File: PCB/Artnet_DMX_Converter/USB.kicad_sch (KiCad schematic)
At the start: 3 parts, among them J2 USB_C_Receptacle_USB2.0_14P, U3 USBLC6-2SC6

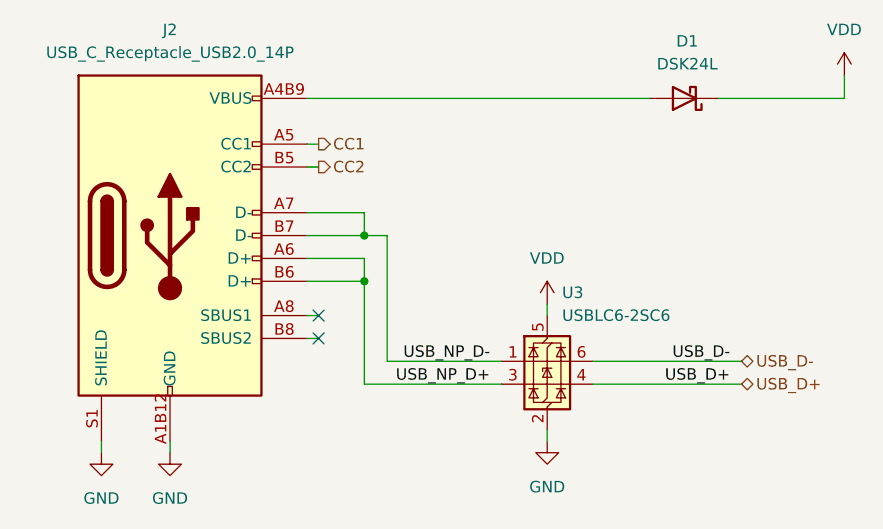
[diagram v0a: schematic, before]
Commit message: Updated the PCB Allot
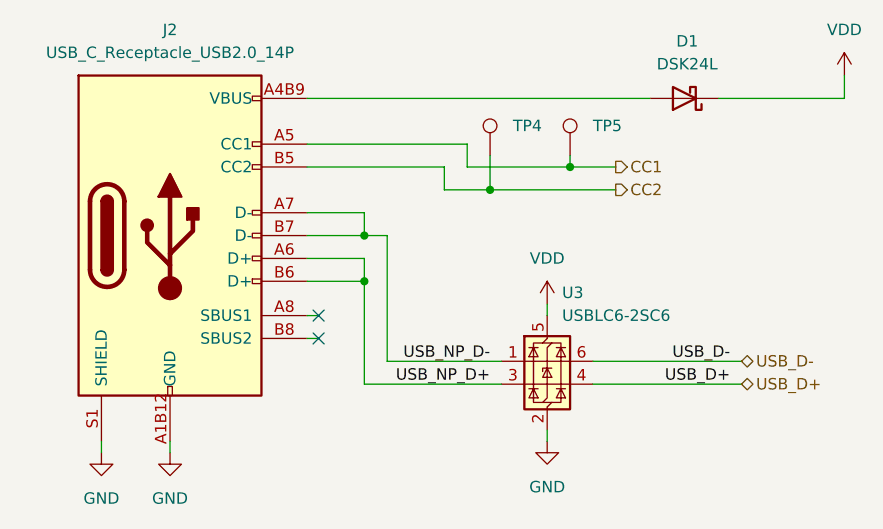
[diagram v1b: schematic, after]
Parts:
- added TP4, TP5: TestPoint, TestPoint:TestPoint_Pad_D1.5mm, symbol Connector:TestPoint
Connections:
- net CC1: now also TP5.1
- net CC2: now also TP4.1
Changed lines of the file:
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@@
+	)
+	(junction
+		(at 125.73 81.28)
+		(diameter 0)
+		(color 0 0 0 0)
 	)
 	(junction
@@
 	)
 	(junction
+		(at 116.84 83.82)
+		(diameter 0)
+		(color 0 0 0 0)
+	)
+	(junction
 		(at 102.87 93.98)
 		(diameter 0)
@@
 	(wire
 		(pts
+			(xy 116.84 83.82) (xy 130.81 83.82)
+		)
+		(stroke
+			(width 0)
+			(type default)
+		)
+	)
+	(wire
+		(pts
 			(xy 102.87 93.98) (xy 102.87 105.41)
 		)
@@
 	(wire
 		(pts
+			(xy 114.3 81.28) (xy 114.3 78.74)
+		)
+		(stroke
+			(width 0)
+			(type default)
+		)
+	)
+	(wire
+		(pts
 			(xy 123.19 111.76) (xy 123.19 110.49)
 		)
@@
 	(wire
 		(pts
-			(xy 96.52 81.28) (xy 97.79 81.28)
+			(xy 111.76 83.82) (xy 116.84 83.82)
 		)
 		(stroke
@@
 	(wire
 		(pts
-			(xy 96.52 78.74) (xy 97.79 78.74)
+			(xy 114.3 81.28) (xy 125.73 81.28)
+		)
+		(stroke
+			(width 0)
+			(type default)
+		)
+	)
+	(wire
+		(pts
+			(xy 96.52 78.74) (xy 114.3 78.74)
 		)
 		(stroke
@@
 	(wire
 		(pts
+			(xy 111.76 83.82) (xy 111.76 81.28)
+		)
+		(stroke
+			(width 0)
+			(type default)
+		)
+	)
+	(wire
+		(pts
 			(xy 96.52 100.33) (xy 97.79 100.33)
 		)
@@
 	(wire
 		(pts
+			(xy 116.84 80.01) (xy 116.84 83.82)
+		)
+		(stroke
+			(width 0)
+			(type default)
+		)
+	)
+	(wire
+		(pts
 			(xy 105.41 88.9) (xy 102.87 88.9)
 		)
@@
 	(wire
 		(pts
+			(xy 125.73 81.28) (xy 130.81 81.28)
+		)
+		(stroke
+			(width 0)
+			(type default)
+		)
+	)
+	(wire
+		(pts
+			(xy 96.52 81.28) (xy 111.76 81.28)
+		)
+		(stroke
+			(width 0)
+			(type default)
+		)
+	)
+	(wire
+		(pts
 			(xy 105.41 102.87) (xy 105.41 88.9)
 		)
@@
 		(pts
 			(xy 96.52 86.36) (xy 102.87 86.36)
+		)
+		(stroke
+			(width 0)
+			(type default)
+		)
+	)
+	(wire
+		(pts
+			(xy 125.73 80.01) (xy 125.73 81.28)
 		)
 		(stroke
@@
 	(hierarchical_label "CC1"
 		(shape output)
-		(at 97.79 78.74 0)
+		(at 130.81 81.28 0)
 		(effects
 			(font
@@
 	(hierarchical_label "CC2"
 		(shape output)
-		(at 97.79 81.28 0)
+		(at 130.81 83.82 0)
 		(effects
 			(font
@@
 		(dnp no)
 		(fields_autoplaced yes)
-		(property "Reference" "#PWR029"
+		(property "Reference" "#PWR027"
 			(at 81.28 119.38 0)
 			(effects
@@
 			(project "Artnet_DMX_Converter"
 				(path "/7d5b1976-98b3-4e47-ae52-3fe360235ea3/29cdc2ff-67bb-4206-b190-ec0480ab55fd"
-					(reference "#PWR029")
+					(reference "#PWR027")
 					(unit 1)
 				)
@@
 	)
 	(symbol
+		(lib_id "Connector:TestPoint")
+		(at 125.73 80.01 0)
+		(unit 1)
+		(exclude_from_sim no)
+		(in_bom yes)
+		(on_board yes)
+		(dnp no)
+		(property "Reference" "TP5"
+			(at 128.27 76.7079 0)
+			(effects
+				(font
+					(size 1.27 1.27)
+				)
+				(justify left)
+			)
+		)
+		(property "Value" "TestPoint"
+			(at 128.27 77.9779 0)
+			(effects
+				(font
+					(size 1.27 1.27)
+				)
+				(justify left)
+				(hide yes)
+			)
+		)
+		(property "Footprint" "TestPoint:TestPoint_Pad_D1.5mm"
+			(at 130.81 80.01 0)
+			(effects
+				(font
+					(size 1.27 1.27)
+				)
+				(hide yes)
+			)
+		)
+		(property "Datasheet" "~"
+			(at 130.81 80.01 0)
+			(effects
+				(font
+					(size 1.27 1.27)
+				)
+				(hide yes)
+			)
+		)
+		(property "Description" "test point"
+			(at 125.73 80.01 0)
+			(effects
+				(font
+					(size 1.27 1.27)
+				)
+				(hide yes)
+			)
+		)
+		(pin "1"
+		)
+		(instances
+			(project "Artnet_DMX_Converter"
+				(path "/7d5b1976-98b3-4e47-ae52-3fe360235ea3/29cdc2ff-67bb-4206-b190-ec0480ab55fd"
+					(reference "TP5")
+					(unit 1)
+				)
+			)
+		)
+	)
+	(symbol
 		(lib_id "power:VDD")
 		(at 123.19 96.52 0)
@@
 		(dnp no)
 		(fields_autoplaced yes)
-		(property "Reference" "#PWR026"
+		(property "Reference" "#PWR024"
 			(at 123.19 100.33 0)
 			(effects
@@
 			(project "Artnet_DMX_Converter"
 				(path "/7d5b1976-98b3-4e47-ae52-3fe360235ea3/29cdc2ff-67bb-4206-b190-ec0480ab55fd"
-					(reference "#PWR026")
+					(reference "#PWR024")
 					(unit 1)
 				)
@@
 		(dnp no)
 		(fields_autoplaced yes)
-		(property "Reference" "#PWR028"
+		(property "Reference" "#PWR026"
 			(at 73.66 119.38 0)
 			(effects
@@
 			(project "Artnet_DMX_Converter"
 				(path "/7d5b1976-98b3-4e47-ae52-3fe360235ea3/29cdc2ff-67bb-4206-b190-ec0480ab55fd"
-					(reference "#PWR028")
+					(reference "#PWR026")
 					(unit 1)
 				)
@@
 		(dnp no)
 		(fields_autoplaced yes)
-		(property "Reference" "#PWR027"
+		(property "Reference" "#PWR025"
 			(at 123.19 118.11 0)
 			(effects
@@
 			(project "Artnet_DMX_Converter"
 				(path "/7d5b1976-98b3-4e47-ae52-3fe360235ea3/29cdc2ff-67bb-4206-b190-ec0480ab55fd"
-					(reference "#PWR027")
+					(reference "#PWR025")
 					(unit 1)
 				)
@@
 					(unit 1)
 				)
+			)
+		)
+	)
+	(symbol
+		(lib_id "Connector:TestPoint")
+		(at 116.84 80.01 0)
+		(unit 1)
+		(exclude_from_sim no)
+		(in_bom yes)
+		(on_board yes)
+		(dnp no)
+		(property "Reference" "TP4"
+			(at 119.38 76.7079 0)
+			(effects
+				(font
+					(size 1.27 1.27)
+				)
+				(justify left)
+			)
+		)
+		(property "Value" "TestPoint"
+			(at 119.38 77.9779 0)
+			(effects
+				(font
+					(size 1.27 1.27)
+				)
+				(justify left)
+				(hide yes)
+			)
+		)
+		(property "Footprint" "TestPoint:TestPoint_Pad_D1.5mm"
+			(at 121.92 80.01 0)
+			(effects
+				(font
+					(size 1.27 1.27)
+				)
+				(hide yes)
+			)
+		)
+		(property "Datasheet" "~"
+			(at 121.92 80.01 0)
+			(effects
+				(font
+					(size 1.27 1.27)
+				)
+				(hide yes)
+			)
+		)
+		(property "Description" "test point"
+			(at 116.84 80.01 0)
+			(effects
+				(font
+					(size 1.27 1.27)
+				)
+				(hide yes)
+			)
+		)
+		(pin "1"
+		)
+		(instances
+			(project "Artnet_DMX_Converter"
+				(path "/7d5b1976-98b3-4e47-ae52-3fe360235ea3/29cdc2ff-67bb-4206-b190-ec0480ab55fd"
+					(reference "TP4")
+					(unit 1)
+				)
